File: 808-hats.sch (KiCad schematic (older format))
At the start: 54 parts, among them J5 trig/accent, J6 output, P1 MTA-156-4, Q1 BC546, Q10 BC546, Q2 BC546, Q3 BC556, Q4 BC556, Q5 BC546, Q6 BC546, Q7 BC546, Q8 BC546, Q9 BC546

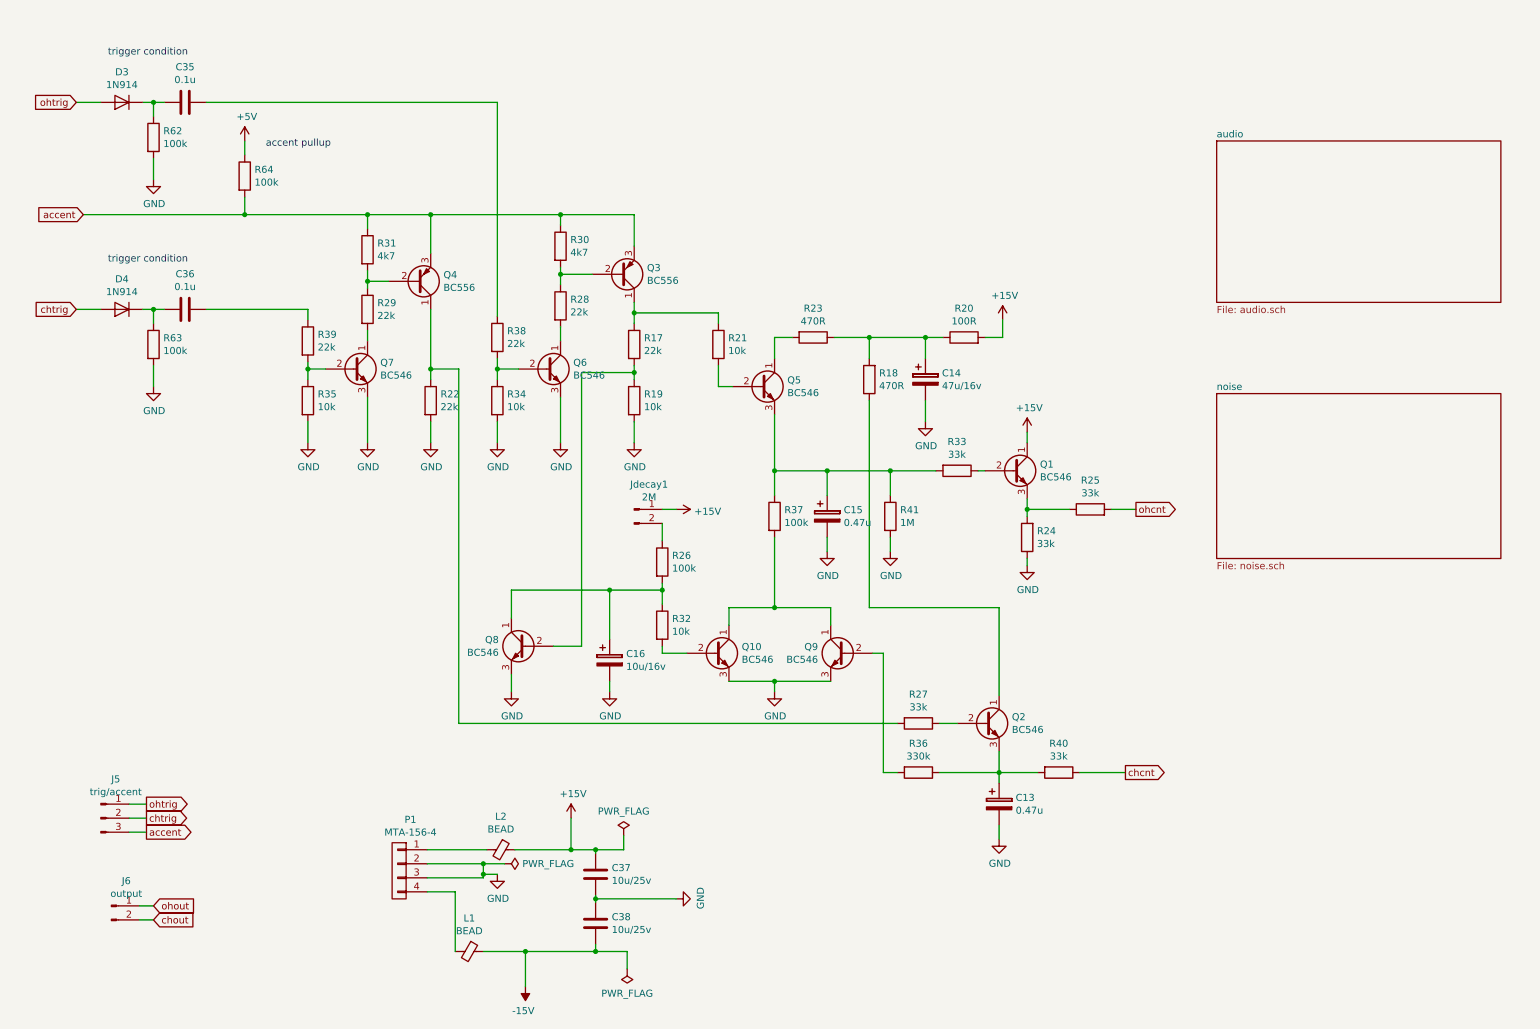
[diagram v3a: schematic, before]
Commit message: added hex-inverter style trigger conditioning (amplification?)
https://static1.squarespace.com/static/54c8f37ae4b015761b133d43/550b9d69e4b0c859c95703b9/550b9d69e4b0c859c95703ba/1426824558402/NeinOhNein_KICK_v1_schem.png?format=2500w
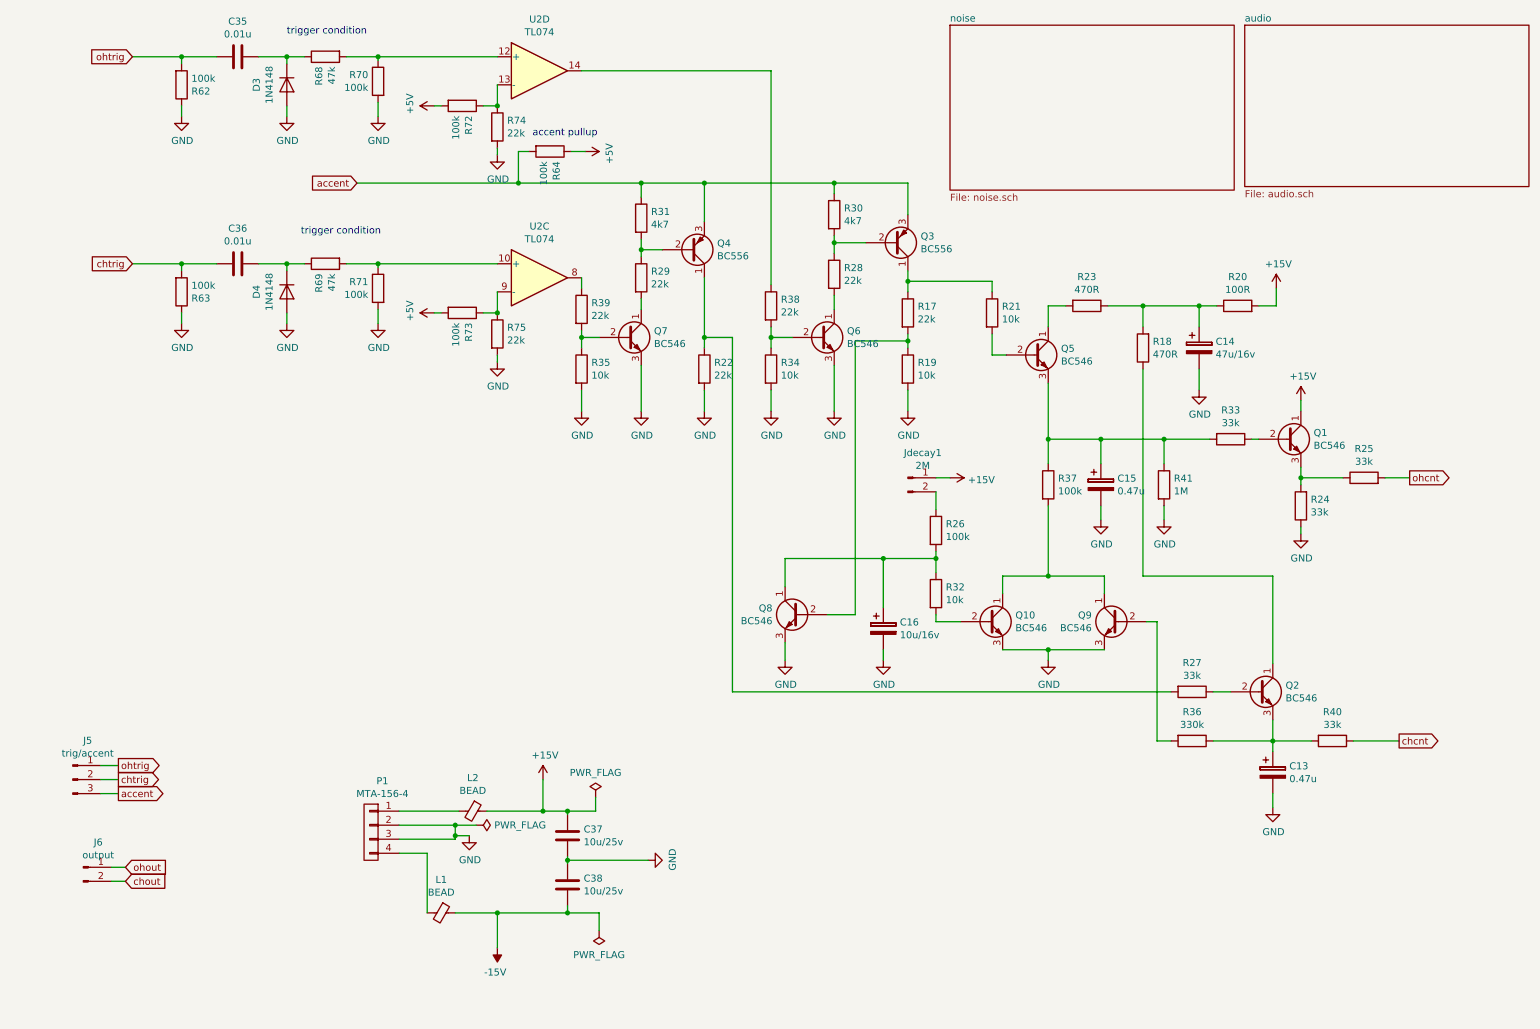
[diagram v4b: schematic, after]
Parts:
- added R68, R69: 47k, symbol Device:R
- added R70, R71, R72, R73: 100k, symbol Device:R
- added R74, R75: 22k, symbol Device:R
- added U2: TL074, symbol Amplifier_Operational:TL074
- C35, C36: value 0.1u -> 0.01u
- D3, D4: value 1N914 -> 1N4148
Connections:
- net +5V: now also R72.2, R73.2
- net GND: now also D3.2 (A), D4.2 (A), R62.1, R63.1, R70.2, R71.2, R74.2, R75.2; no longer R62.2, R63.2
- net chtrig: now also C36.2, R63.2; no longer D4.2 (A)
- net ohtrig: now also C35.2, R62.2; no longer D3.2 (A)
- net at R38.1: now also U2.14; no longer C35.1
- net at R39.1: now also U2.8; no longer C36.1
- new net: C36.1, D4.1 (K), R69.1
- new net: R69.2, R71.1, U2.10 (+)
- new net: R73.1, R75.1, U2.9 (-)
- new net: C35.1, D3.1 (K), R68.1
- new net: R68.2, R70.1, U2.12 (+)
- new net: R72.1, R74.1, U2.13 (-)
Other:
- moved on the sheet: C13, C14, C15, C16, C36, C37, C38, D4, J5, J6, Jdecay1, L1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

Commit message: cleanup
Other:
- moved on the sheet: R64
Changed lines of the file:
@@
 Text GLabel 1200 2250 0    50   Input ~ 0
 chtrig
-Text GLabel 2800 1675 0    50   Input ~ 0
+Text GLabel 1225 1675 0    50   Input ~ 0
 accent
 Wire Wire Line
@@
 Wire Wire Line
 	4825 2150 4825 2200
-Wire Wire Line
-	2800 1675 3950 1675
 Wire Wire Line
 	4825 1675 4825 1775
@@
 L Device:R R64
 U 1 1 5CB59E4A
-P 4175 1450
-F 0 "R64" H 4245 1496 50  0000 L CNN
-F 1 "100k" H 4245 1405 50  0000 L CNN
-F 2 "" V 4105 1450 50  0001 C CNN
-F 3 "~" H 4175 1450 50  0001 C CNN
-	1    4175 1450
-	0    1    1    0
-$EndComp
-Connection ~ 3950 1675
-Wire Wire Line
-	3950 1675 4825 1675
+P 1275 1475
+F 0 "R64" H 1345 1521 50  0000 L CNN
+F 1 "100k" H 1345 1430 50  0000 L CNN
+F 2 "" V 1205 1475 50  0001 C CNN
+F 3 "~" H 1275 1475 50  0001 C CNN
+	1    1275 1475
+	1    0    0    -1
+$EndComp
 $Comp
 L power:+5V #PWR03
 U 1 1 5CB5DC8A
-P 4425 1450
-F 0 "#PWR03" H 4425 1300 50  0001 C CNN
-F 1 "+5V" H 4440 1623 50  0000 C CNN
-F 2 "" H 4425 1450 50  0001 C CNN
-F 3 "" H 4425 1450 50  0001 C CNN
-	1    4425 1450
-	0    1    1    0
-$EndComp
-Wire Wire Line
-	4425 1450 4325 1450
-Text Notes 4050 1350 0    50   ~ 0
+P 1275 1225
+F 0 "#PWR03" H 1275 1075 50  0001 C CNN
+F 1 "+5V" H 1290 1398 50  0000 C CNN
+F 2 "" H 1275 1225 50  0001 C CNN
+F 3 "" H 1275 1225 50  0001 C CNN
+	1    1275 1225
+	1    0    0    -1
+$EndComp
+Wire Wire Line
+	1275 1225 1275 1325
+Text Notes 1175 1600 1    50   ~ 0
 accent pullup
 $Comp
@@
 	4400 875  5750 875
 Wire Wire Line
-	4025 1450 3950 1450
-Wire Wire Line
-	3950 1450 3950 1675
-Wire Wire Line
 	3800 775  2950 775
+Wire Wire Line
+	1225 1675 1275 1675
+Wire Wire Line
+	1275 1625 1275 1675
+Connection ~ 1275 1675
+Wire Wire Line
+	1275 1675 4825 1675
 $EndSCHEMATC

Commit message: selected some parts
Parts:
- C14, C16: footprint (none) -> Capacitor_THT:CP_Radial_D7.5mm_P2.50mm
- J5: footprint (none) -> Connector_PinHeader_2.54mm:PinHeader_1x03_P2.54mm_Vertical
- J6, Jdecay1: footprint (none) -> Connector_PinHeader_2.54mm:PinHeader_1x02_P2.54mm_Vertical
- Q1, Q10, Q2, Q3, Q4, Q5, Q6, Q7, Q8, Q9: footprint Package_TO_SOT_THT:TO-92_Inline -> Package_TO_SOT_THT:TO-92L_Inline
- R17, R18, R19, R20, R21, R22, R23, R24, R25, R26, R27, R28, R29, R30, R31, R32, R33, R34, R35, R36, R37, R38, R39, R40, R41, R62, R63, R64, R68, R69, R70, R71, R72, R73, R74, R75: footprint (none) -> Resistor_THT:R_Axial_DIN0204_L3.6mm_D1.6mm_P7.62mm_Horizontal
- U2: footprint (none) -> Package_DIP:DIP-14_W7.62mm_LongPads

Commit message: assigned footprints
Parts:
- C13, C15: footprint (none) -> Capacitor_THT:CP_Radial_D7.5mm_P2.50mm
- C35, C36: footprint (none) -> Capacitor_THT:C_Rect_L7.2mm_W3.0mm_P5.00mm_FKS2_FKP2_MKS2_MKP2
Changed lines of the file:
@@
 F 0 "C15" H 8218 3871 50  0000 L CNN
 F 1 "0.47u" H 8218 3780 50  0000 L CNN
-F 2 "" H 8138 3675 50  0001 C CNN
+F 2 "Capacitor_THT:CP_Radial_D7.5mm_P2.50mm" H 8138 3675 50  0001 C CNN
 F 3 "~" H 8100 3825 50  0001 C CNN
 	1    8100 3825
@@
 F 0 "C13" H 9443 5921 50  0000 L CNN
 F 1 "0.47u" H 9443 5830 50  0000 L CNN
-F 2 "" H 9363 5725 50  0001 C CNN
+F 2 "Capacitor_THT:CP_Radial_D7.5mm_P2.50mm" H 9363 5725 50  0001 C CNN
 F 3 "~" H 9325 5875 50  0001 C CNN
 	1    9325 5875
@@
 F 0 "C36" V 1698 2250 50  0000 C CNN
 F 1 "0.01u" V 1789 2250 50  0000 C CNN
-F 2 "" H 1988 2100 50  0001 C CNN
+F 2 "Capacitor_THT:C_Rect_L7.2mm_W3.0mm_P5.00mm_FKS2_FKP2_MKS2_MKP2" H 1988 2100 50  0001 C CNN
 F 3 "~" H 1950 2250 50  0001 C CNN
 	1    1950 2250
@@
 F 0 "C35" V 1698 775 50  0000 C CNN
 F 1 "0.01u" V 1789 775 50  0000 C CNN
-F 2 "" H 1988 625 50  0001 C CNN
+F 2 "Capacitor_THT:C_Rect_L7.2mm_W3.0mm_P5.00mm_FKS2_FKP2_MKS2_MKP2" H 1988 625 50  0001 C CNN
 F 3 "~" H 1950 775 50  0001 C CNN
 	1    1950 775

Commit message: oops, through hole for bead
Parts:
- L1, L2: footprint Inductor_SMD:L_0603_1608Metric_Pad1.05x0.95mm_HandSolder -> Resistor_THT:R_Axial_DIN0207_L6.3mm_D2.5mm_P10.16mm_Horizontal
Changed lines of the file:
@@
 F 0 "L2" V 3388 6150 50  0000 C CNN
 F 1 "BEAD" V 3479 6150 50  0000 C CNN
-F 2 "Inductor_SMD:L_0603_1608Metric_Pad1.05x0.95mm_HandSolder" V 3555 6150 50  0001 C CNN
+F 2 "Resistor_THT:R_Axial_DIN0207_L6.3mm_D2.5mm_P10.16mm_Horizontal" V 3555 6150 50  0001 C CNN
 F 3 "~" H 3625 6150 50  0001 C CNN
 	1    3625 6150
@@
 F 0 "L1" V 3163 6875 50  0000 C CNN
 F 1 "BEAD" V 3254 6875 50  0000 C CNN
-F 2 "Inductor_SMD:L_0603_1608Metric_Pad1.05x0.95mm_HandSolder" V 3330 6875 50  0001 C CNN
+F 2 "Resistor_THT:R_Axial_DIN0207_L6.3mm_D2.5mm_P10.16mm_Horizontal" V 3330 6875 50  0001 C CNN
 F 3 "~" H 3400 6875 50  0001 C CNN
 	1    3400 6875
